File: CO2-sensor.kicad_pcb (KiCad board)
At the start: 2 copper layers, 41 parts, among them IC1 SCD41-D-R1, IC2 NCP1117ST33T3G, IC3 W25Q32JVSSIQ, J1 1734028-1, U1 RP2040, Y1 ABM8-272-T3

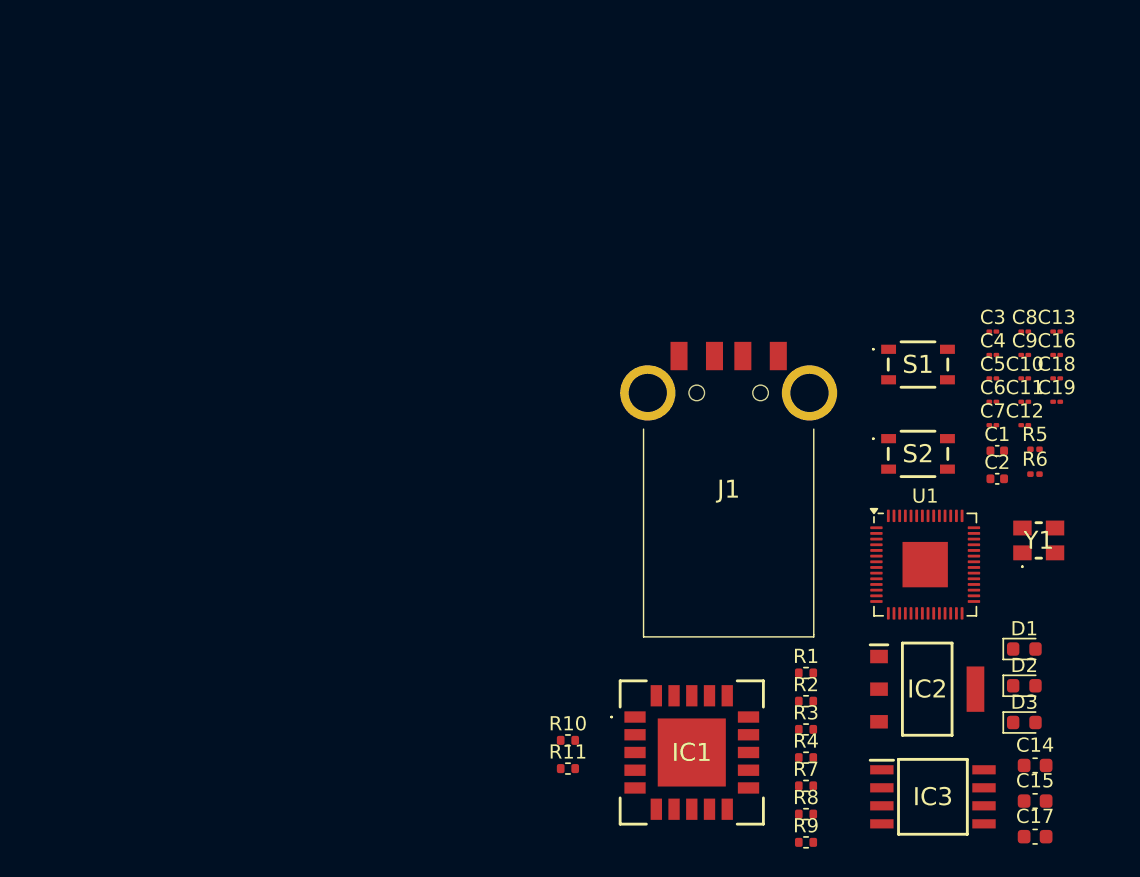
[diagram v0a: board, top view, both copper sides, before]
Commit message: removed components folder
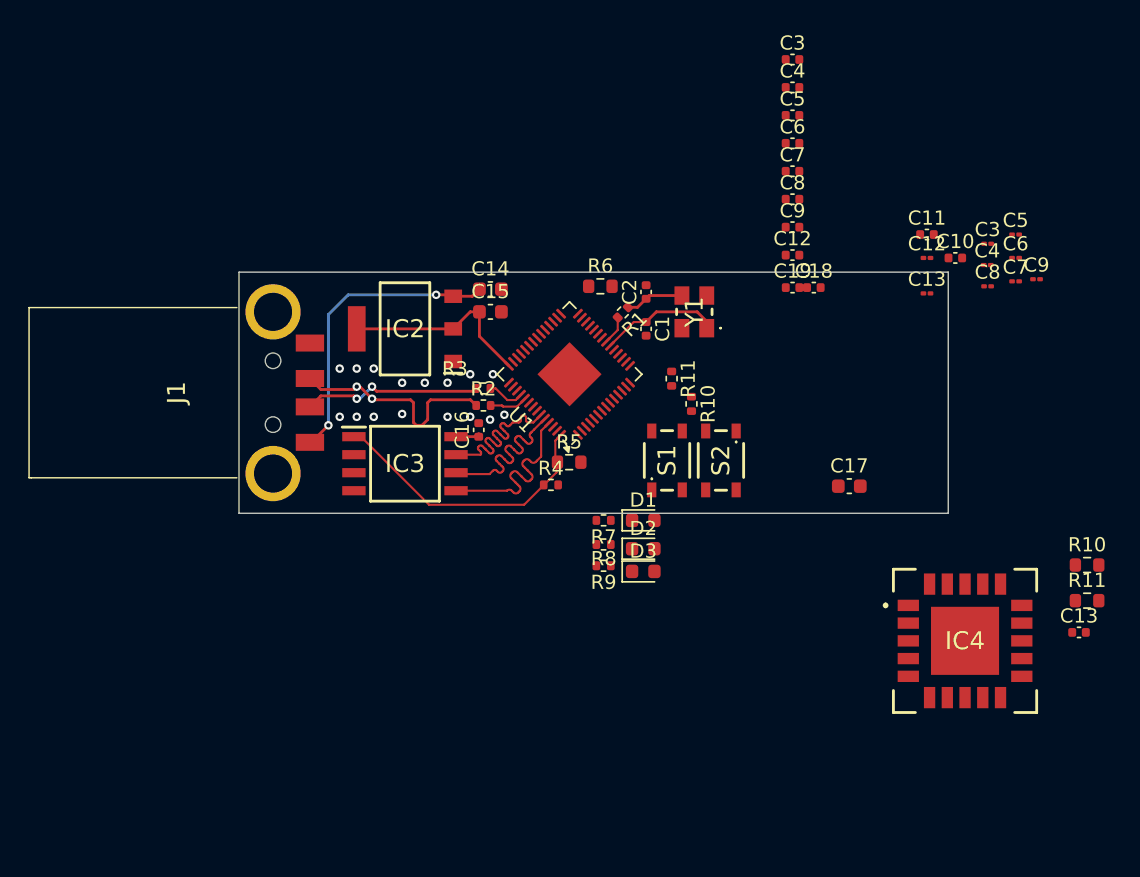
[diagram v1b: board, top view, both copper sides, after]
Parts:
- removed IC1: SCD41-D-R1, Imported_parts:SCD41DR1
- added C12: 100n, Capacitor_SMD:C_0402_1005Metric, F.Cu at (84.5, 35.8)
- added C13: 1u, Capacitor_SMD:C_0402_1005Metric, F.Cu at (104.7, 62.4)
- added C3: 100n, Capacitor_SMD:C_0402_1005Metric, F.Cu at (84.5, 22.0)
- added C4: 100n, Capacitor_SMD:C_0402_1005Metric, F.Cu at (84.5, 24.0)
- added C5: 100n, Capacitor_SMD:C_0402_1005Metric, F.Cu at (84.5, 25.9)
- added C6: 100n, Capacitor_SMD:C_0402_1005Metric, F.Cu at (84.5, 27.9)
- added C7: 100n, Capacitor_SMD:C_0402_1005Metric, F.Cu at (84.5, 29.9)
- added C8: 100n, Capacitor_SMD:C_0402_1005Metric, F.Cu at (84.5, 31.9)
- added C9: 100n, Capacitor_SMD:C_0402_1005Metric, F.Cu at (84.5, 33.8)
- added IC4: SCD40-D-R2, Imported_parts:SCD40DR2, F.Cu at (96.7, 63.0)
- added R10: 10k, Resistor_SMD:R_0603_1608Metric, F.Cu at (105.3, 57.6)
- added R11: 10k, Resistor_SMD:R_0603_1608Metric, F.Cu at (105.3, 60.2)
- C10, C11, C16, C18, C19: footprint Capacitor_SMD:C_01005_0402Metric -> Capacitor_SMD:C_0402_1005Metric
- R5, R6: footprint Resistor_SMD:R_0201_0603Metric -> Resistor_SMD:R_0603_1608Metric
- moved C15 51.6 mm to (63.2, 39.8)
- moved C14 51.0 mm to (63.2, 38.2)
- moved IC2 44.7 mm to (57.2, 41.0), turned to 180 degrees
- moved IC3 44.0 mm to (57.2, 50.5)
- moved C16 41.1 mm to (62.4, 48.1), turned to 90 degrees
- moved J1 40.1 mm to (40.6, 45.5), turned to -90 degrees
- moved R6 33.4 mm to (71.0, 38.0)
- moved R3 33.1 mm to (62.7, 45.2)
- moved R5 32.9 mm to (68.8, 50.4)
- moved R2 30.9 mm to (62.7, 46.4)
- moved Y1 29.1 mm to (77.6, 39.8), turned to 90 degrees
- moved D3 28.9 mm to (74.0, 58.1)
- moved D2 28.5 mm to (74.0, 56.5)
- moved R1 28.5 mm to (72.6, 39.8), turned to -135 degrees
- moved R11 28.4 mm to (76.0, 44.5), turned to -90 degrees
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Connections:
- IC2 pad 4: unconnected-(IC2-OUTPUT_2-Pad4) -> +3.3V
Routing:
- net +5V: track 0.00 -> 21.1 mm, vias 0 -> 2
- net /QSPI_SS: track 0.00 -> 20.1 mm
- net D+: track 0.00 -> 16.1 mm, vias 0 -> 2
- net +3.3V: track 0.00 -> 15.5 mm
- net /QSPI_SD3: track 0.00 -> 13.8 mm
- net /QSPI_SD0: track 0.00 -> 13.7 mm
- net /QSPI_SCLK: track 0.00 -> 13.6 mm
- net D-: track 0.00 -> 13.1 mm, vias 0 -> 2
- net /Xin: track 0.00 -> 8.57 mm
- net Net-(Y1-CRYSTAL_2): track 0.00 -> 4.15 mm
- net Net-(U1-USB_DP): track 0.00 -> 2.69 mm
- net Net-(U1-USB_DM): track 0.00 -> 2.66 mm
- net /Xout: track 0.00 -> 2.05 mm
- net (no net): vias 0 -> 16
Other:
- board outline added: 50 x 17 mm
